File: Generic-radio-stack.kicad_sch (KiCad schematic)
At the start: 22 parts, among them J1 USB_B_Mini, SW1 SW_Push_LED, SW2 SW_Push_LED, SW3 SW_Push_LED, SW4 SW_Push_LED, U1 NCP1117-3.3_SOT223

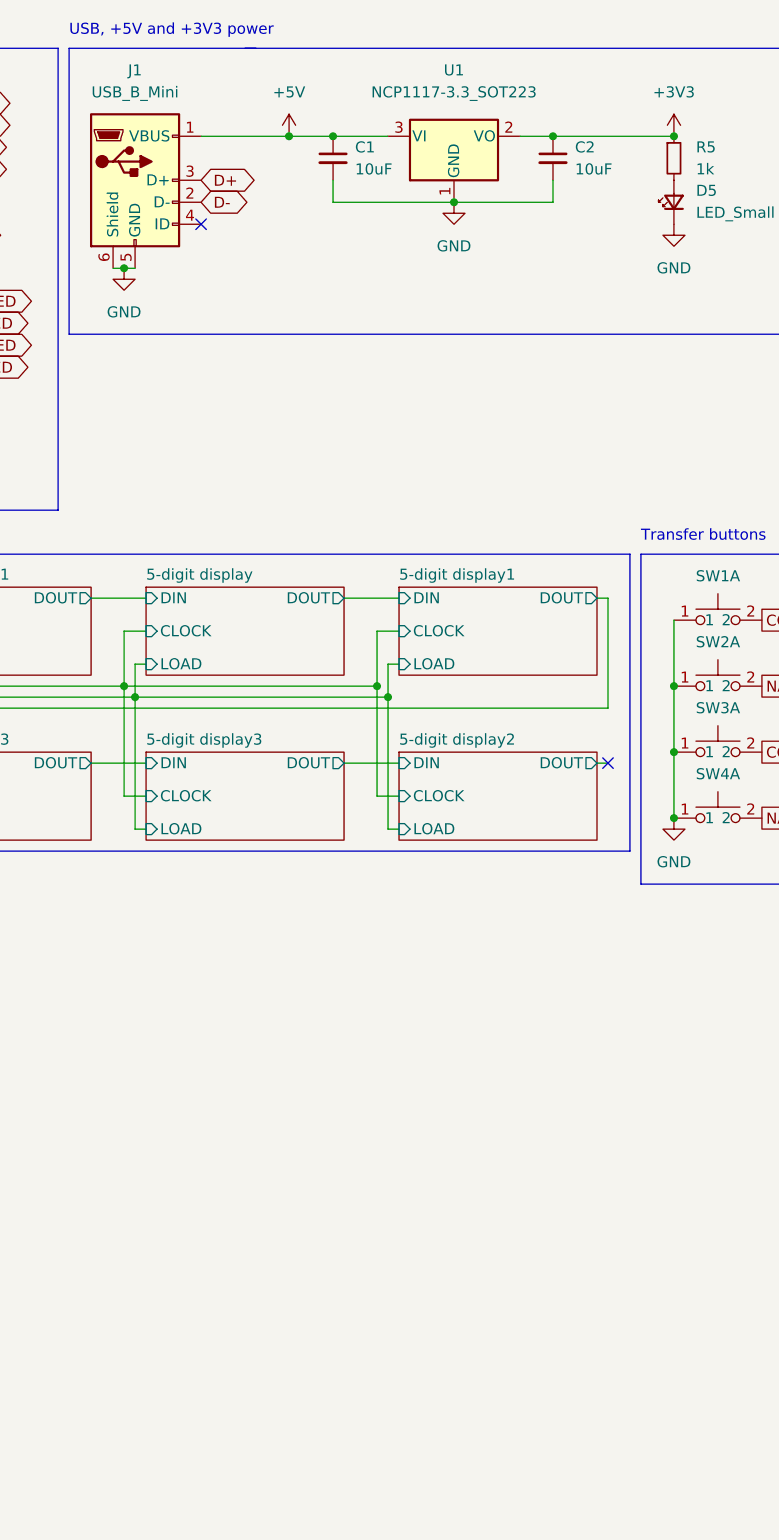
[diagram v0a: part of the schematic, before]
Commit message: Added dual encoder 3d model, fit everything on the board
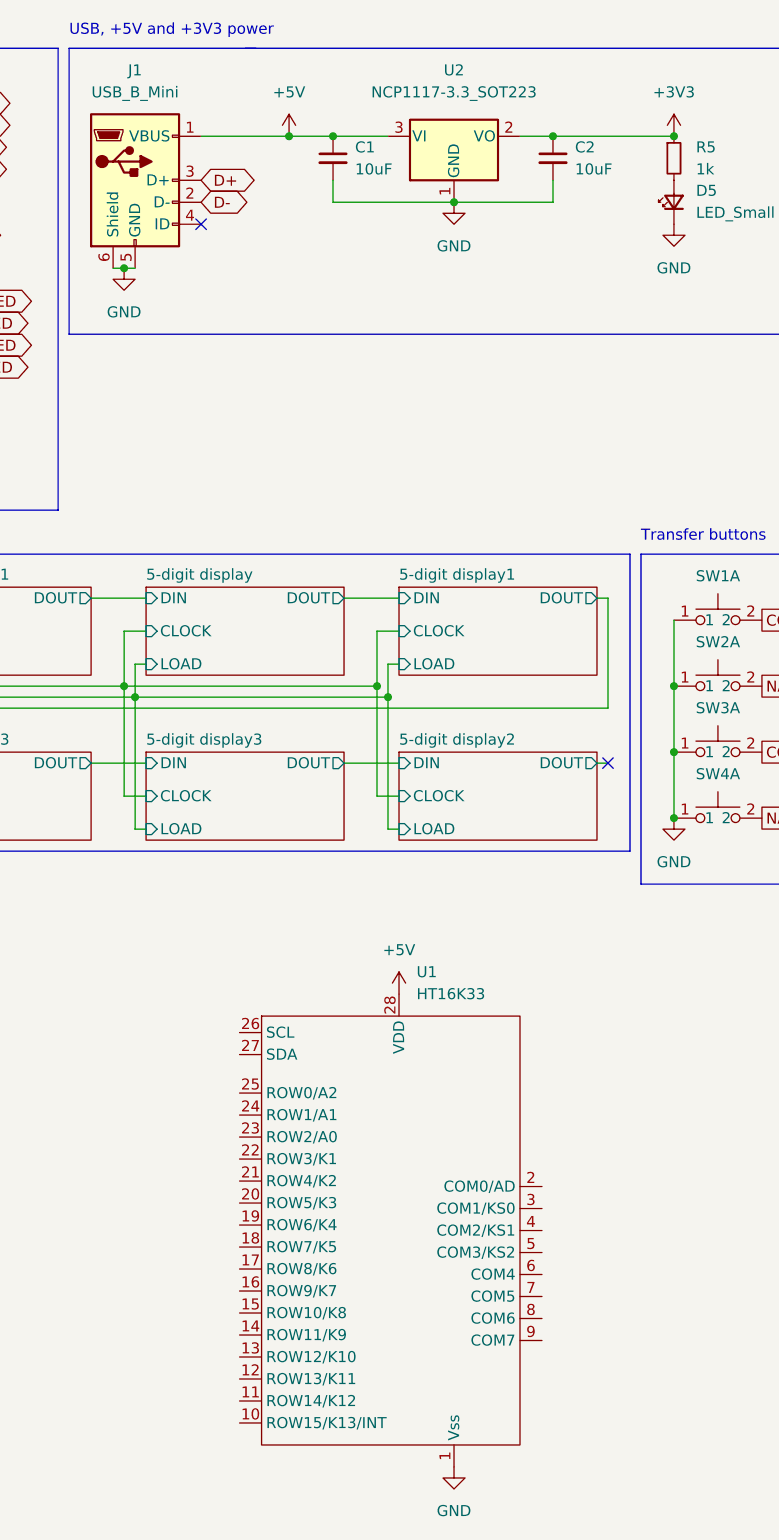
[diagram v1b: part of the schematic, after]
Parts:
- added U1: HT16K33, Generic-radio-stack:SOIC-28, symbol Generic-radio-stack:HT16K33
- D1, D2, D3, D4: footprint LED_THT:LED_D5.0mm -> LED_THT:LED_D3.0mm
- renumbered U1 to U2
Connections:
- net +5V: now also U1.28 (VDD)
- net GND: now also U1.1 (Vss)

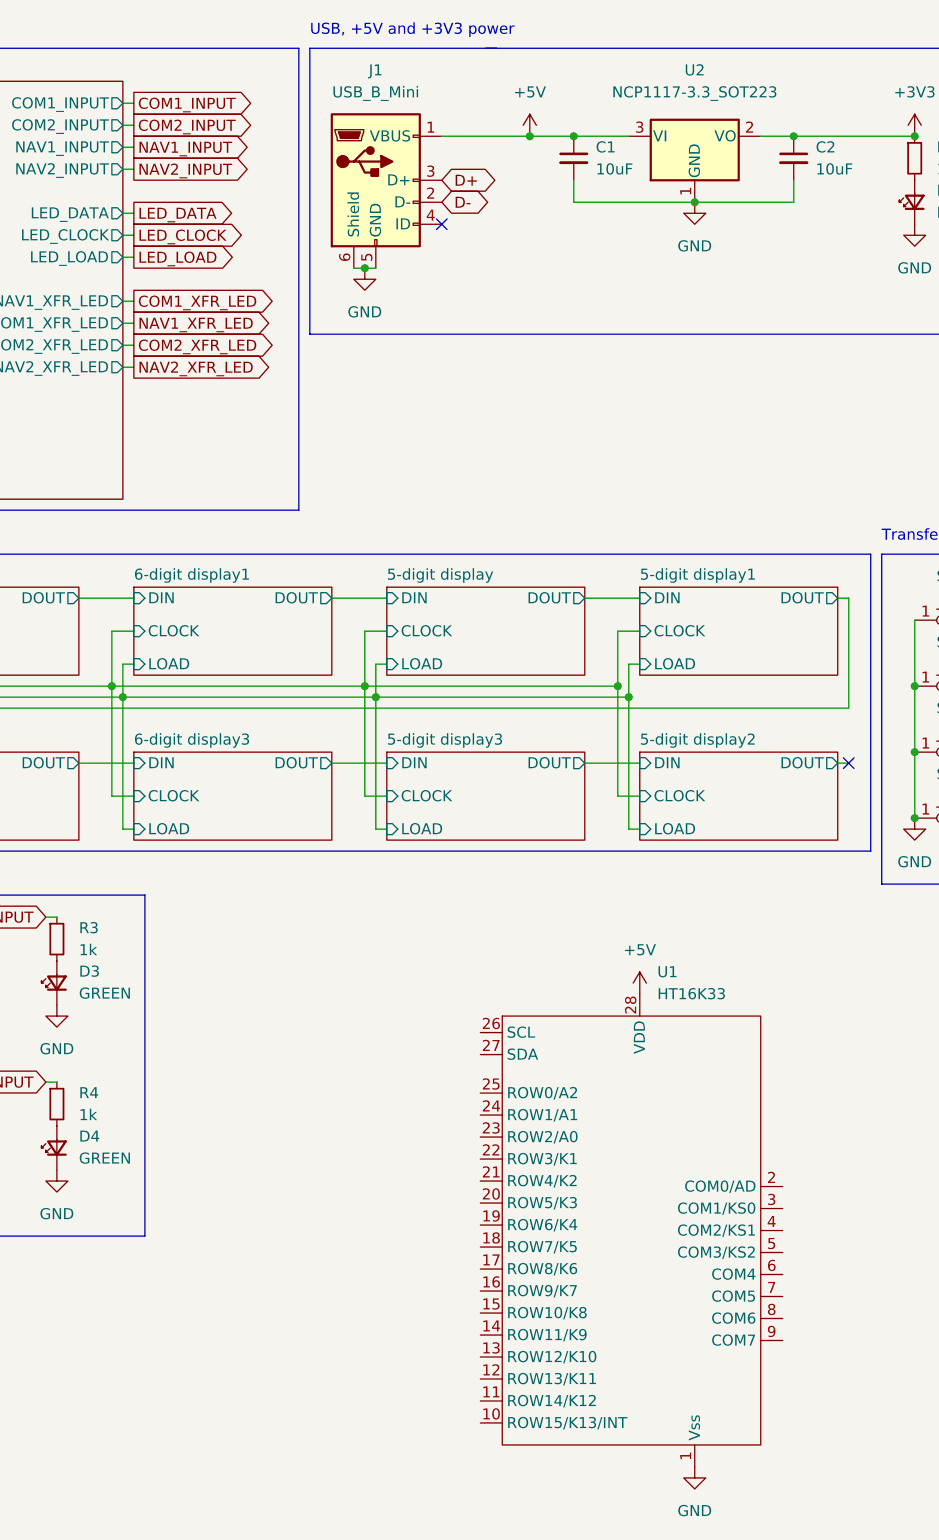
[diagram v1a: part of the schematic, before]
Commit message: Add mounting holes
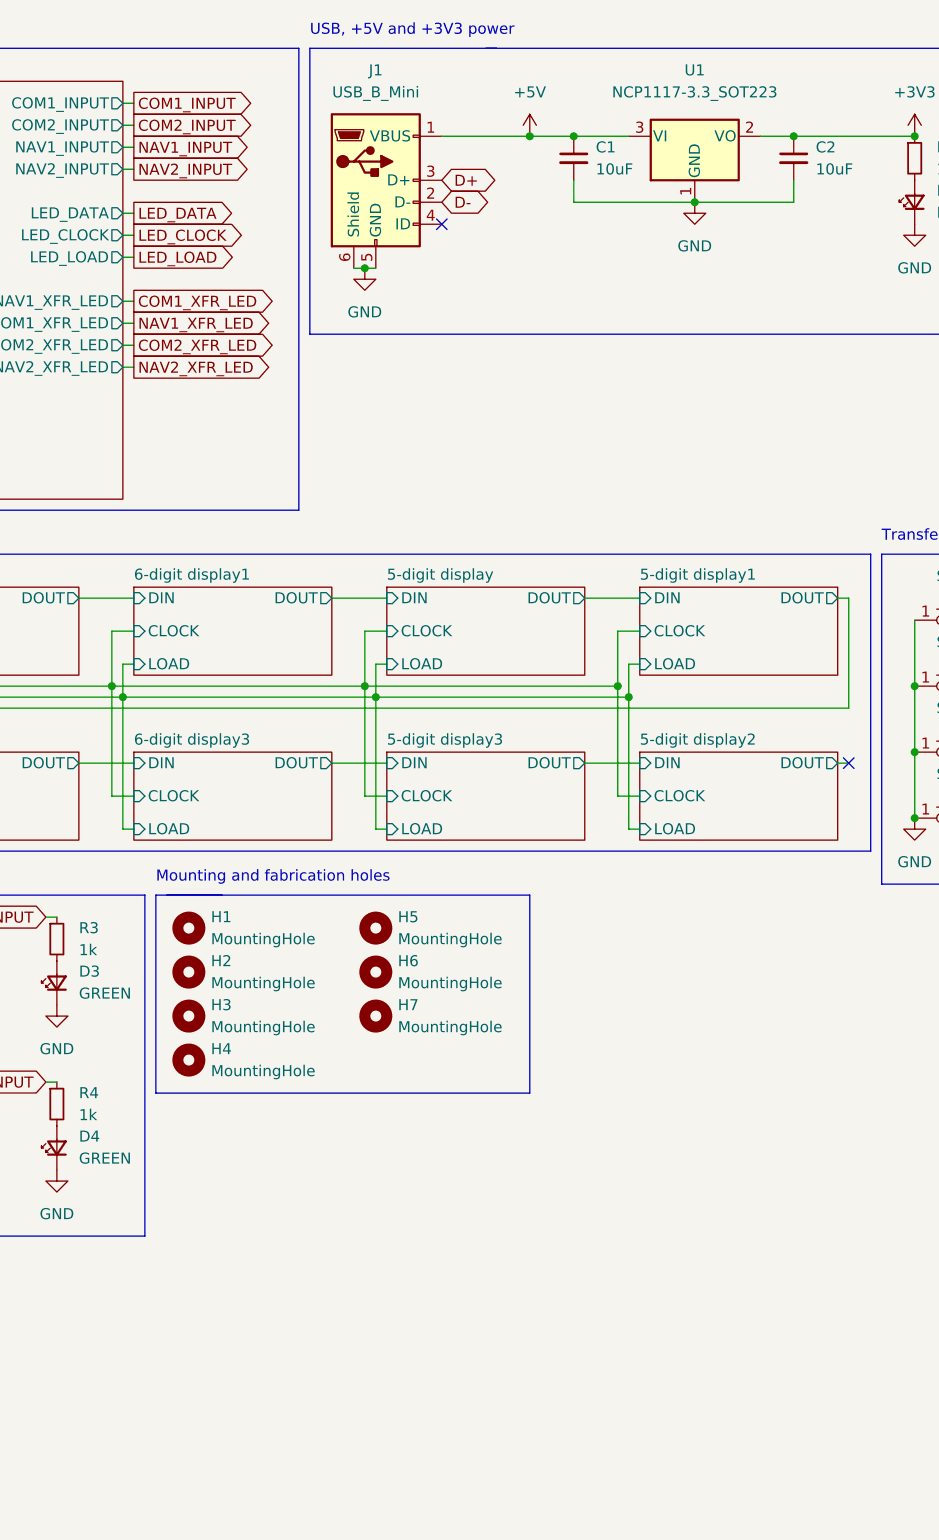
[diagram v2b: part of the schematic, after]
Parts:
- removed U1: HT16K33, Generic-radio-stack:SOIC-28, symbol Generic-radio-stack:HT16K33
- added H1, H2, H3, H4: MountingHole, MountingHole:MountingHole_3.2mm_M3, symbol Mechanical:MountingHole
- added H5, H6, H7: MountingHole, Generic-radio-stack:JLCPCB_Tooling_Hole, symbol Mechanical:MountingHole
- renumbered U2 to U1
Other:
- note added: "Mounting and fabrication holes"

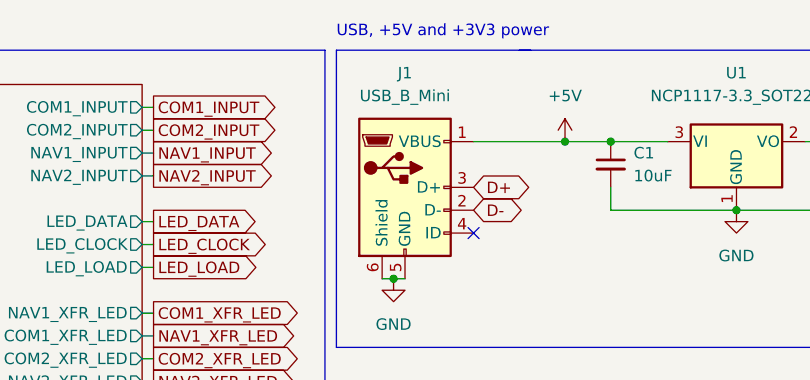
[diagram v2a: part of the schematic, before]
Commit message: New USB footprint
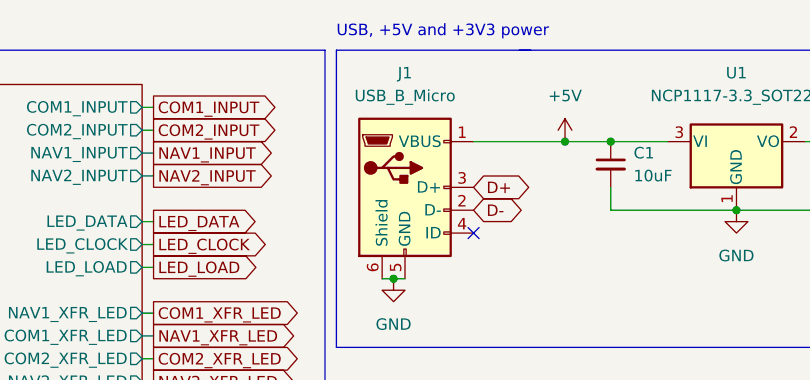
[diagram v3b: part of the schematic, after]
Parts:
- removed J1: USB_B_Mini, Generic-radio-stack:USB_B_Mini_Amphenol_UE25BE5510H, symbol Connector:USB_B_Mini
- added J1: USB_B_Micro, Generic-radio-stack:ZX80-B-5P, symbol Connector:USB_B_Micro
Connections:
- net +5V: now also J1.1 (VBUS)
- net D+: now also J1.3 (D+)
- net D-: now also J1.2 (D-)
- net GND: now also J1.5 (GND), J1.6 (Shield)
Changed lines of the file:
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@@
     (pin "2")
+  )
+  (symbol (lib_id "Connector:USB_B_Micro") (at 91.44 31.75 0) (unit 1)
+    (in_bom yes) (on_board yes) (fields_autoplaced)
+    (property "Reference" "J1" (id 0) (at 91.44 19.05 0))
+    (property "Value" "USB_B_Micro" (id 1) (at 91.44 21.59 0))
+    (property "Footprint" "Generic-radio-stack:ZX80-B-5P" (id 2) (at 95.25 33.02 0)
+      (effects (font (size 1.27 1.27)) hide)
+    )
+    (property "Datasheet" "~" (id 3) (at 95.25 33.02 0)
+      (effects (font (size 1.27 1.27)) hide)
+    )
+    (pin "1")
+    (pin "2")
+    (pin "3")
+    (pin "4")
+    (pin "5")
+    (pin "6")
   )
   (symbol (lib_id "Generic-radio-stack:SW_Push_LED") (at 158.75 96.52 0) (unit 1)
@@
     )
     (pin "1")
-  )
-  (symbol (lib_id "Connector:USB_B_Mini") (at 91.44 31.75 0) (unit 1)
-    (in_bom yes) (on_board yes) (fields_autoplaced)
-    (property "Reference" "J1" (id 0) (at 91.44 19.05 0))
-    (property "Value" "USB_B_Mini" (id 1) (at 91.44 21.59 0))
-    (property "Footprint" "Generic-radio-stack:USB_B_Mini_Amphenol_UE25BE5510H" (id 2) (at 95.25 33.02 0)
-      (effects (font (size 1.27 1.27)) hide)
-    )
-    (property "Datasheet" "~" (id 3) (at 95.25 33.02 0)
-      (effects (font (size 1.27 1.27)) hide)
-    )
-    (pin "1")
-    (pin "2")
-    (pin "3")
-    (pin "4")
-    (pin "5")
-    (pin "6")
   )
   (symbol (lib_id "Device:R_Small") (at 153.67 29.21 0) (unit 1)
@@
       (reference "H7") (unit 1) (value "MountingHole") (footprint "Generic-radio-stack:JLCPCB_Tooling_Hole")
     )
-    (path "/f944e54f-0ecd-410c-b8a8-c34801570847"
-      (reference "J1") (unit 1) (value "USB_B_Mini") (footprint "Generic-radio-stack:USB_B_Mini_Amphenol_UE25BE5510H")
+    (path "/8bb8ae6f-c2e7-453e-8bb9-bb8cfac7befc"
+      (reference "J1") (unit 1) (value "USB_B_Micro") (footprint "Generic-radio-stack:ZX80-B-5P")
     )
     (path "/e46d07d7-cb69-451f-8024-840ce0e84fbe/43959dfc-cde1-43bb-982b-96160d44b42f"
